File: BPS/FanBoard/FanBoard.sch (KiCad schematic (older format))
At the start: 13 parts, among them J1 Conn_01x02, J2 Conn_01x02, J3 Conn_01x02, J4 Conn_01x02, J5 LDRBRDConn, Q1 BUK9M34-100EX, Q2 BUK9M34-100EX, Q3 BUK9M34-100EX, Q4 BUK9M34-100EX

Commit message: Redid layout of board
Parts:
- removed J5: LDRBRDConn, Connector_Molex:Molex_Micro-Fit_3.0_43045-0612_2x03_P3.00mm_Vertical, symbol Connector_Generic:Conn_02x03_Counter_Clockwise
- added H1, H2, H3, H4: MountingHole, MountingHole:MountingHole_3mm, symbol Mechanical:MountingHole
- added J5: LDRBRDConn, Connector_Molex:Molex_Micro-Fit_3.0_43045-0612_2x03_P3.00mm_Vertical, symbol Connector_Generic:Conn_02x03_Top_Bottom
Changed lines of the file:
@@
-$EndComp
-$Comp
-L Connector_Generic:Conn_02x03_Counter_Clockwise J5
-U 1 1 5F1BA642
-P 1300 4850
-F 0 "J5" H 1350 5200 50  0000 C CNN
-F 1 "LDRBRDConn" H 1350 5100 50  0000 C CNN
-F 2 "Connector_Molex:Molex_Micro-Fit_3.0_43045-0612_2x03_P3.00mm_Vertical" H 1300 4850 50  0001 C CNN
-F 3 "~" H 1300 4850 50  0001 C CNN
-	1    1300 4850
-	1    0    0    -1
 $EndComp
 $Comp
@@
 	0    1    1    0
 $EndComp
+$Comp
+L Mechanical:MountingHole H1
+U 1 1 5F1DFA7F
+P 5300 3650
+F 0 "H1" H 5400 3696 50  0000 L CNN
+F 1 "MountingHole" H 5400 3605 50  0000 L CNN
+F 2 "MountingHole:MountingHole_3mm" H 5300 3650 50  0001 C CNN
+F 3 "~" H 5300 3650 50  0001 C CNN
+	1    5300 3650
+	1    0    0    -1
+$EndComp
+$Comp
+L Mechanical:MountingHole H2
+U 1 1 5F1E031B
+P 5300 3950
+F 0 "H2" H 5400 3996 50  0000 L CNN
+F 1 "MountingHole" H 5400 3905 50  0000 L CNN
+F 2 "MountingHole:MountingHole_3mm" H 5300 3950 50  0001 C CNN
+F 3 "~" H 5300 3950 50  0001 C CNN
+	1    5300 3950
+	1    0    0    -1
+$EndComp
+$Comp
+L Mechanical:MountingHole H3
+U 1 1 5F1E06E8
+P 5300 4250
+F 0 "H3" H 5400 4296 50  0000 L CNN
+F 1 "MountingHole" H 5400 4205 50  0000 L CNN
+F 2 "MountingHole:MountingHole_3mm" H 5300 4250 50  0001 C CNN
+F 3 "~" H 5300 4250 50  0001 C CNN
+	1    5300 4250
+	1    0    0    -1
+$EndComp
+$Comp
+L Mechanical:MountingHole H4
+U 1 1 5F1E0A9F
+P 5300 4600
+F 0 "H4" H 5400 4646 50  0000 L CNN
+F 1 "MountingHole" H 5400 4555 50  0000 L CNN
+F 2 "MountingHole:MountingHole_3mm" H 5300 4600 50  0001 C CNN
+F 3 "~" H 5300 4600 50  0001 C CNN
+	1    5300 4600
+	1    0    0    -1
+$EndComp
+$Comp
+L Connector_Generic:Conn_02x03_Top_Bottom J5
+U 1 1 5F1EEC57
+P 1300 4850
+F 0 "J5" H 1350 5167 50  0000 C CNN
+F 1 "LDRBRDConn" H 1350 5076 50  0000 C CNN
+F 2 "Connector_Molex:Molex_Micro-Fit_3.0_43045-0612_2x03_P3.00mm_Vertical" H 1300 4850 50  0001 C CNN
+F 3 "~" H 1300 4850 50  0001 C CNN
+	1    1300 4850
+	1    0    0    -1
+$EndComp
 $EndSCHEMATC

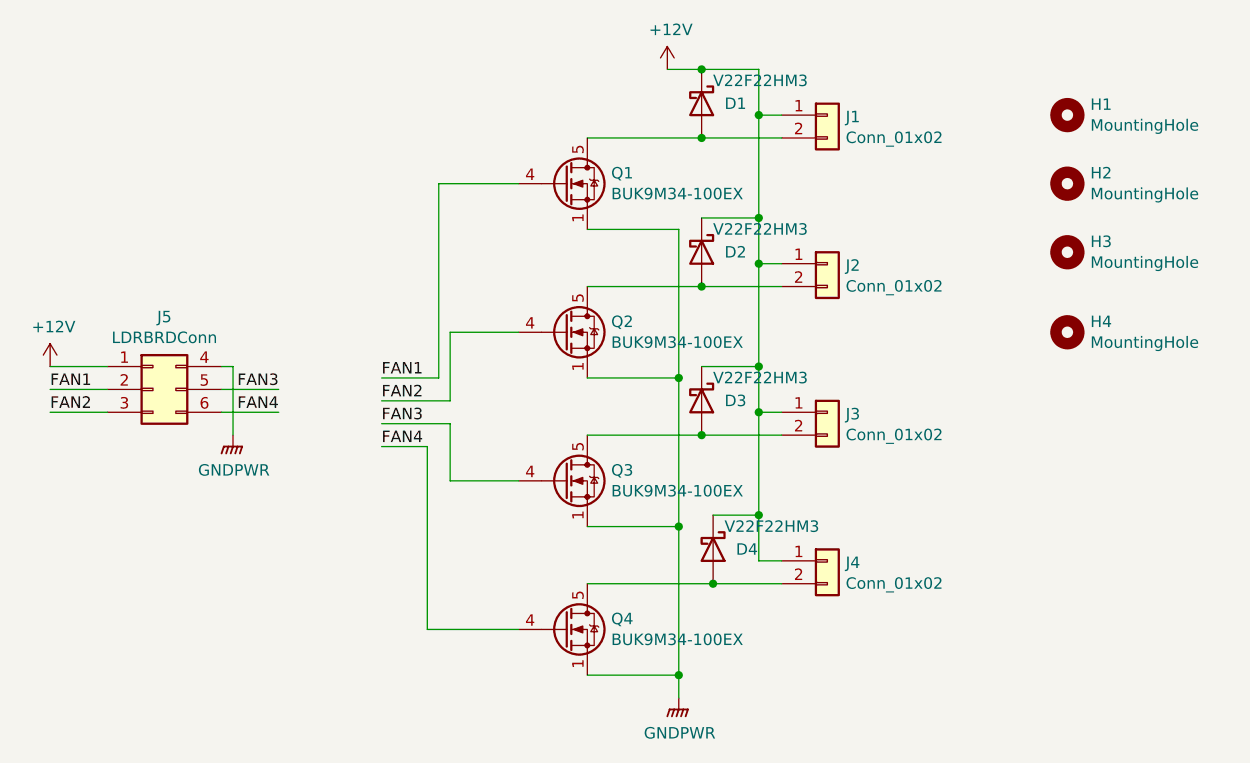
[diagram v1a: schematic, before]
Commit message: Added status LED
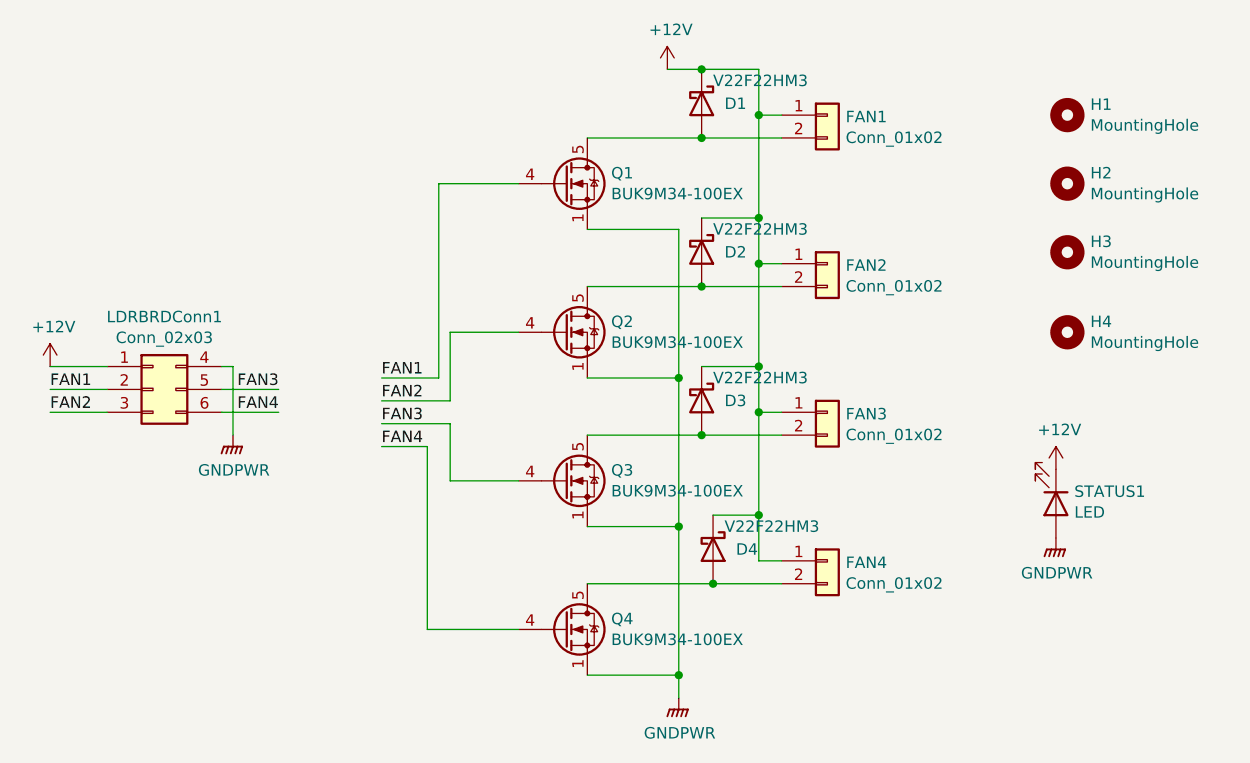
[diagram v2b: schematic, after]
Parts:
- added STATUS1: LED, LED_SMD:LED_0805_2012Metric, symbol Device:LED
- LDRBRDConn1: renamed from J5; value LDRBRDConn -> Conn_02x03
- renumbered J1 to FAN1, J2 to FAN2, J3 to FAN3, J4 to FAN4
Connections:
- net +12V: now also STATUS1.1 (K)
- net GNDPWR: now also STATUS1.2 (A)
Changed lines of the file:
@@
 $EndDescr
-$Comp
-L Connector_Generic:Conn_01x02 J1
-U 1 1 5F091D5D
-P 4250 3650
-F 0 "J1" H 4330 3642 50  0000 L CNN
-F 1 "Conn_01x02" H 4330 3551 50  0000 L CNN
-F 2 "UTSVT_Connectors:Molex_MicroFit3.0_1x2xP3.00mm_PolarizingPeg_Vertical" H 4250 3650 50  0001 C CNN
-F 3 "~" H 4250 3650 50  0001 C CNN
-	1    4250 3650
-	1    0    0    -1
-$EndComp
-$Comp
-L Connector_Generic:Conn_01x02 J2
-U 1 1 5F09203F
-P 4250 4300
-F 0 "J2" H 4330 4292 50  0000 L CNN
-F 1 "Conn_01x02" H 4330 4201 50  0000 L CNN
-F 2 "UTSVT_Connectors:Molex_MicroFit3.0_1x2xP3.00mm_PolarizingPeg_Vertical" H 4250 4300 50  0001 C CNN
-F 3 "~" H 4250 4300 50  0001 C CNN
-	1    4250 4300
-	1    0    0    -1
-$EndComp
-$Comp
-L Connector_Generic:Conn_01x02 J3
-U 1 1 5F092588
-P 4250 4950
-F 0 "J3" H 4330 4942 50  0000 L CNN
-F 1 "Conn_01x02" H 4330 4851 50  0000 L CNN
-F 2 "UTSVT_Connectors:Molex_MicroFit3.0_1x2xP3.00mm_PolarizingPeg_Vertical" H 4250 4950 50  0001 C CNN
-F 3 "~" H 4250 4950 50  0001 C CNN
-	1    4250 4950
-	1    0    0    -1
-$EndComp
-$Comp
-L Connector_Generic:Conn_01x02 J4
-U 1 1 5F092946
-P 4250 5600
-F 0 "J4" H 4330 5592 50  0000 L CNN
-F 1 "Conn_01x02" H 4330 5501 50  0000 L CNN
-F 2 "UTSVT_Connectors:Molex_MicroFit3.0_1x2xP3.00mm_PolarizingPeg_Vertical" H 4250 5600 50  0001 C CNN
-F 3 "~" H 4250 5600 50  0001 C CNN
-	1    4250 5600
-	1    0    0    -1
-$EndComp
 $Comp
 L power:+12V #PWR01
@@
 $EndComp
 $Comp
-L Connector_Generic:Conn_02x03_Top_Bottom J5
+L Connector_Generic:Conn_02x03_Top_Bottom LDRBRDConn1
 U 1 1 5F1EEC57
 P 1300 4850
-F 0 "J5" H 1350 5167 50  0000 C CNN
-F 1 "LDRBRDConn" H 1350 5076 50  0000 C CNN
+F 0 "LDRBRDConn1" H 1350 5167 50  0000 C CNN
+F 1 "Conn_02x03" H 1350 5076 50  0000 C CNN
 F 2 "Connector_Molex:Molex_Micro-Fit_3.0_43045-0612_2x03_P3.00mm_Vertical" H 1300 4850 50  0001 C CNN
 F 3 "~" H 1300 4850 50  0001 C CNN
@@
 	1    0    0    -1
 $EndComp
+$Comp
+L Device:LED STATUS1
+U 1 1 5F1F72F0
+P 5250 5350
+F 0 "STATUS1" V 5197 5430 50  0000 L CNN
+F 1 "LED" V 5288 5430 50  0000 L CNN
+F 2 "LED_SMD:LED_0805_2012Metric" H 5250 5350 50  0001 C CNN
+F 3 "~" H 5250 5350 50  0001 C CNN
+	1    5250 5350
+	0    1    1    0
+$EndComp
+$Comp
+L power:+12V #PWR02
+U 1 1 5F1F79F1
+P 5250 5200
+F 0 "#PWR02" H 5250 5050 50  0001 C CNN
+F 1 "+12V" H 5265 5373 50  0000 C CNN
+F 2 "" H 5250 5200 50  0001 C CNN
+F 3 "" H 5250 5200 50  0001 C CNN
+	1    5250 5200
+	1    0    0    -1
+$EndComp
+$Comp
+L power:GNDPWR #PWR05
+U 1 1 5F1F7EC5
+P 5250 5500
+F 0 "#PWR05" H 5250 5300 50  0001 C CNN
+F 1 "GNDPWR" H 5254 5346 50  0000 C CNN
+F 2 "" H 5250 5450 50  0001 C CNN
+F 3 "" H 5250 5450 50  0001 C CNN
+	1    5250 5500
+	1    0    0    -1
+$EndComp
+$Comp
+L Connector_Generic:Conn_01x02 FAN4
+U 1 1 5F092946
+P 4250 5600
+F 0 "FAN4" H 4330 5592 50  0000 L CNN
+F 1 "Conn_01x02" H 4330 5501 50  0000 L CNN
+F 2 "UTSVT_Connectors:Molex_MicroFit3.0_1x2xP3.00mm_PolarizingPeg_Vertical" H 4250 5600 50  0001 C CNN
+F 3 "~" H 4250 5600 50  0001 C CNN
+	1    4250 5600
+	1    0    0    -1
+$EndComp
+$Comp
+L Connector_Generic:Conn_01x02 FAN3
+U 1 1 5F092588
+P 4250 4950
+F 0 "FAN3" H 4330 4942 50  0000 L CNN
+F 1 "Conn_01x02" H 4330 4851 50  0000 L CNN
+F 2 "UTSVT_Connectors:Molex_MicroFit3.0_1x2xP3.00mm_PolarizingPeg_Vertical" H 4250 4950 50  0001 C CNN
+F 3 "~" H 4250 4950 50  0001 C CNN
+	1    4250 4950
+	1    0    0    -1
+$EndComp
+$Comp
+L Connector_Generic:Conn_01x02 FAN2
+U 1 1 5F09203F
+P 4250 4300
+F 0 "FAN2" H 4330 4292 50  0000 L CNN
+F 1 "Conn_01x02" H 4330 4201 50  0000 L CNN
+F 2 "UTSVT_Connectors:Molex_MicroFit3.0_1x2xP3.00mm_PolarizingPeg_Vertical" H 4250 4300 50  0001 C CNN
+F 3 "~" H 4250 4300 50  0001 C CNN
+	1    4250 4300
+	1    0    0    -1
+$EndComp
+$Comp
+L Connector_Generic:Conn_01x02 FAN1
+U 1 1 5F091D5D
+P 4250 3650
+F 0 "FAN1" H 4330 3642 50  0000 L CNN
+F 1 "Conn_01x02" H 4330 3551 50  0000 L CNN
+F 2 "UTSVT_Connectors:Molex_MicroFit3.0_1x2xP3.00mm_PolarizingPeg_Vertical" H 4250 3650 50  0001 C CNN
+F 3 "~" H 4250 3650 50  0001 C CNN
+	1    4250 3650
+	1    0    0    -1
+$EndComp

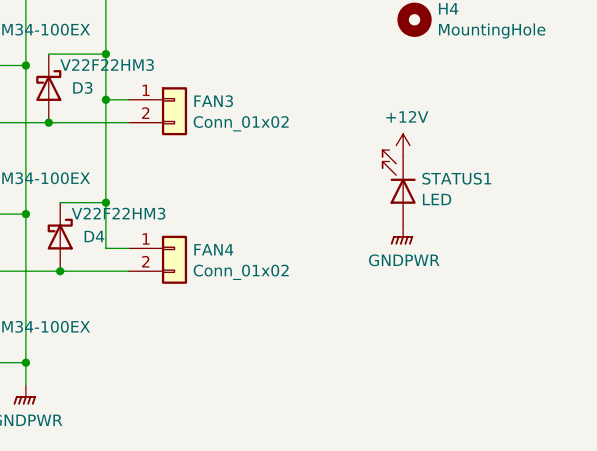
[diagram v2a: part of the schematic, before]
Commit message: Added silkscreen comments
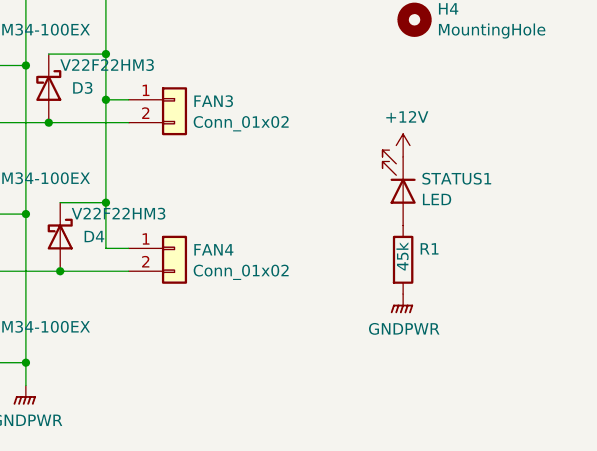
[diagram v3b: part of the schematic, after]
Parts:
- added R1: 45k, Resistor_SMD:R_0805_2012Metric, symbol Device:R
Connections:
- net GNDPWR: now also R1.2; no longer STATUS1.2 (A)
- new net: R1.1, STATUS1.2 (A)
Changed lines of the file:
@@
 L power:GNDPWR #PWR05
 U 1 1 5F1F7EC5
-P 5250 5500
-F 0 "#PWR05" H 5250 5300 50  0001 C CNN
-F 1 "GNDPWR" H 5254 5346 50  0000 C CNN
-F 2 "" H 5250 5450 50  0001 C CNN
-F 3 "" H 5250 5450 50  0001 C CNN
-	1    5250 5500
+P 5250 5800
+F 0 "#PWR05" H 5250 5600 50  0001 C CNN
+F 1 "GNDPWR" H 5254 5646 50  0000 C CNN
+F 2 "" H 5250 5750 50  0001 C CNN
+F 3 "" H 5250 5750 50  0001 C CNN
+	1    5250 5800
 	1    0    0    -1
 $EndComp
@@
 	1    0    0    -1
 $EndComp
+$Comp
+L Device:R R1
+U 1 1 5F1F6C18
+P 5250 5650
+F 0 "R1" H 5320 5696 50  0000 L CNN
+F 1 "45k" V 5250 5600 50  0000 L CNN
+F 2 "Resistor_SMD:R_0805_2012Metric" V 5180 5650 50  0001 C CNN
+F 3 "~" H 5250 5650 50  0001 C CNN
+	1    5250 5650
+	1    0    0    -1
+$EndComp
